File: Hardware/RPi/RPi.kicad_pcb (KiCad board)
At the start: 2 copper layers, 90 parts, among them P1 USB_B, P10 Solder_Pad, P11 Solder_Pad, P12 Solder_Pad, P13 Solder_Pad, P14 Solder_Pad, P15 Solder_Pad, P16 Solder_Pad, P17 Solder_Pad, P18 Solder_Pad, P19 Solder_Pad, P2 CONN_01X06, P3 USB_A, P4 USB_A, P5 USB_A, P6 USB_A, P7 Solder_Pad, P8 Solder_Pad, P9 Solder_Pad, U1 MPU_9150, U10 WS2812B, U11 WS2812B, U12 WS2812B, U13 Teensy_LC, U14 WS2812B, U15 WS2812B, U16 WS2812B, U17 WS2812B, U18 WS2812B, U19 WS2812B, U2 RPi_Interface, U3 FE1.1s, U4 AP1117E25, U5 Dual_buffer_NC7WZ16, U6 ESP-12E, U7 WS2812B, U8 WS2812B, U9 WS2812B, Y1 Crystal 12MHz

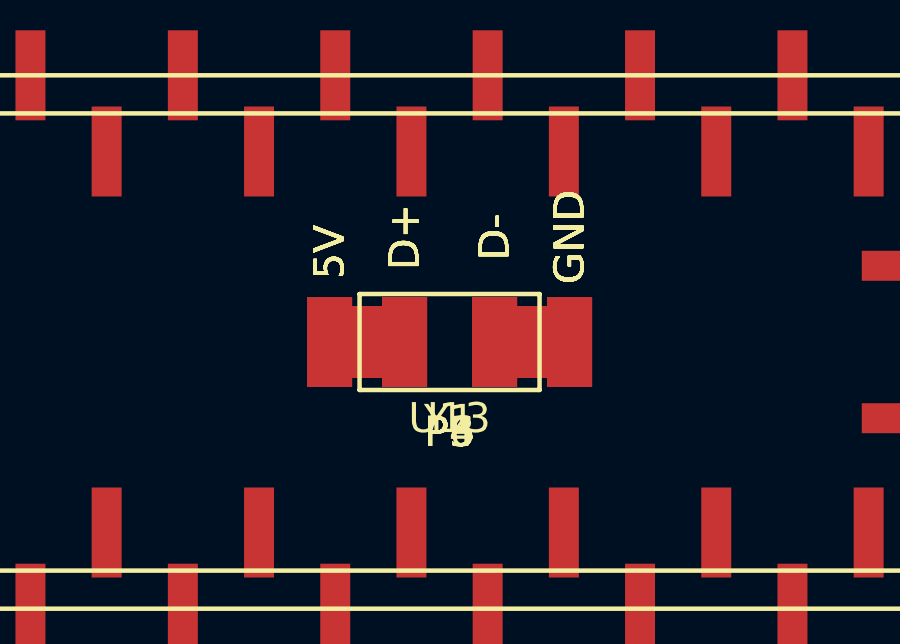
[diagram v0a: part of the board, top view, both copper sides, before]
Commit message: Fixed schematic/component errors
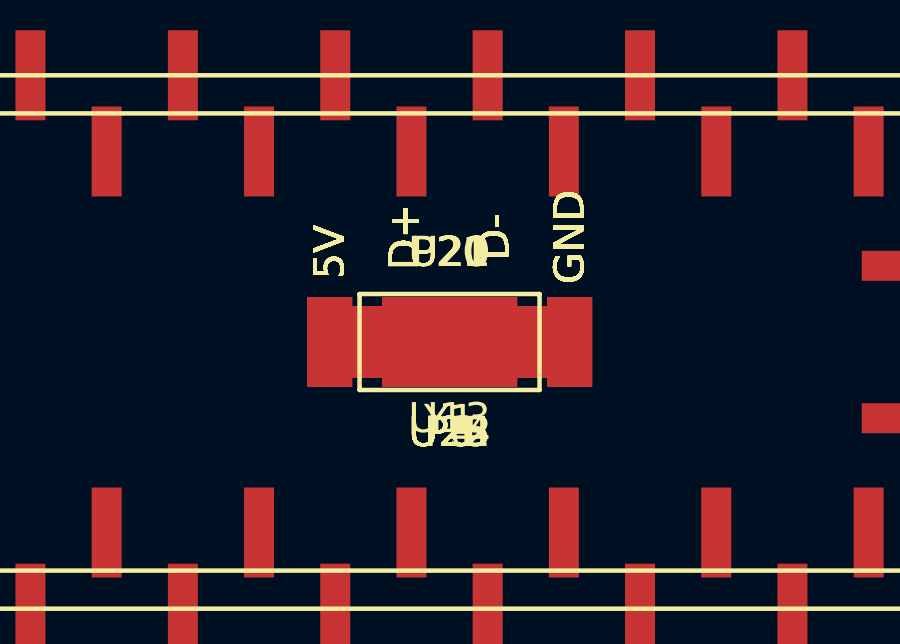
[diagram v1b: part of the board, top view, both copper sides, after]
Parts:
- added P20, P21: Solder_Pad, Measurement_Points:Measurement_Point_Square-SMD-Pad_Big, F.Cu at (0.00, 0.00)
- added U20, U21: SolderpadPowerOut, Measurement_Points:Measurement_Point_Square-SMD-Pad_Big, F.Cu at (0.00, 0.00)
- added U22, U23, U24, U25: USB_Solder_Pad, TimeArc:USB_A_SMD_Pads, F.Cu at (0.00, 0.00)
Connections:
- P1 pad 1: +5V -> Net-(P1-Pad1)
- P3 pad 4: GND -> Net-(P3-Pad4)
- P4 pad 4: GND -> Net-(P4-Pad4)
- P5 pad 4: GND -> Net-(P5-Pad4)
- P6 pad 4: GND -> Net-(P6-Pad4)
- R11 pad 2: Net-(R11-Pad2) -> Net-(P1-Pad1)
- R12 pad 2: Net-(R12-Pad2) -> GND
- R13 pad 2: Net-(R13-Pad2) -> GND
- U13 pad 0: Net-(P7-Pad1) -> (no net)
- U13 pad 1: Net-(P8-Pad1) -> GND
- U13 pad 10: UART_RX -> Net-(U13-Pad10)
- U13 pad 11: Net-(U13-Pad11) -> UART_TX
- U13 pad 12: Net-(U13-Pad12) -> UART_RX
- U13 pad 15: Net-(P19-Pad1) -> WS2812
- U13 pad 16: Net-(P18-Pad1) -> Net-(U13-Pad16)
- U13 pad 17: WS2812 -> GND
- U13 pad 18: Net-(P16-Pad1) -> Net-(U13-Pad18)
- U13 pad 2: Net-(U13-Pad2) -> Net-(P7-Pad1)
- U13 pad 22: Net-(P15-Pad1) -> Net-(P19-Pad1)
- U13 pad 23: Net-(P14-Pad1) -> Net-(P18-Pad1)
- U13 pad 24: (no net) -> Net-(P17-Pad1)
- U13 pad 25: (no net) -> Net-(P16-Pad1)
- U13 pad 27: (no net) -> Net-(U13-Pad27)
- U13 pad 28: (no net) -> Net-(U13-Pad28)
- U13 pad 3: Net-(P9-Pad1) -> Net-(P8-Pad1)
- U13 pad 32: (no net) -> GND
- U13 pad 33: (no net) -> +5V
- U13 pad 4: Net-(P10-Pad1) -> Net-(U13-Pad4)
- U13 pad 5: Net-(U13-Pad5) -> Net-(P9-Pad1)
- U13 pad 6: Net-(U13-Pad6) -> Net-(P10-Pad1)
- U13 pad 9: UART_TX -> Net-(U13-Pad9)
- U2 pad 17: +3V3 -> Net-(U2-Pad17)
- U3 pad 10: Net-(P4-Pad2) -> Net-(U22-Pad2)
- U3 pad 11: Net-(P4-Pad3) -> Net-(U22-Pad3)
- U3 pad 4: Net-(P3-Pad2) -> Net-(U23-Pad2)
- U3 pad 5: Net-(P3-Pad3) -> Net-(U23-Pad3)
- U3 pad 6: Net-(P6-Pad2) -> Net-(U25-Pad2)
- U3 pad 7: Net-(P6-Pad3) -> Net-(U25-Pad3)
- U3 pad 8: Net-(P5-Pad2) -> Net-(U24-Pad2)
- U3 pad 9: Net-(P5-Pad3) -> Net-(U24-Pad3)
- U4 pad 3: Net-(R11-Pad2) -> +5V

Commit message: Starting pcb layout
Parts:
- added REF**: MountingHole_3.2mm_M3_ISO7380, Mounting_Holes:MountingHole_3.2mm_M3_ISO7380, F.Cu at (12.0, 11.0)
- added REF**: MountingHole_3.2mm_M3_ISO7380, Mounting_Holes:MountingHole_3.2mm_M3_ISO7380, F.Cu at (12.0, 97.0)
- added REF**: MountingHole_3.2mm_M3_ISO7380, Mounting_Holes:MountingHole_3.2mm_M3_ISO7380, F.Cu at (98.0, 97.0)
- added REF**: MountingHole_3.2mm_M3_ISO7380, Mounting_Holes:MountingHole_3.2mm_M3_ISO7380, F.Cu at (98.0, 11.0)
- U10, U11, U12, U14, U15, U16, U17, U18, U19, U7, U8, U9: moved to B.Cu
- moved P21 270.4 mm to (269.7, 19.6)
- moved P5 249.1 mm to (249.1, 2.05)
- moved U22 237.9 mm to (237.8, 2.05)
- moved P6 237.0 mm to (236.4, 16.6)
- moved P20 233.4 mm to (226.0, 58.1)
- moved P4 227.1 mm to (226.5, 16.6)
- moved P3 211.9 mm to (208.1, 40.0)
- moved U25 211.3 mm to (209.5, 27.9)
- moved U23 200.9 mm to (194.9, 48.6)
- moved U24 192.6 mm to (182.5, 61.4)
- moved U20 182.2 mm to (175.4, 49.3)
- moved Y1 179.7 mm to (166.9, 66.5)
- moved U21 178.6 mm to (168.7, 58.7)
- moved C1 169.7 mm to (266.9, 26.6)
- moved C6 169.0 mm to (285.9, 6.67)
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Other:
- board outline added: 100 x 100 mm

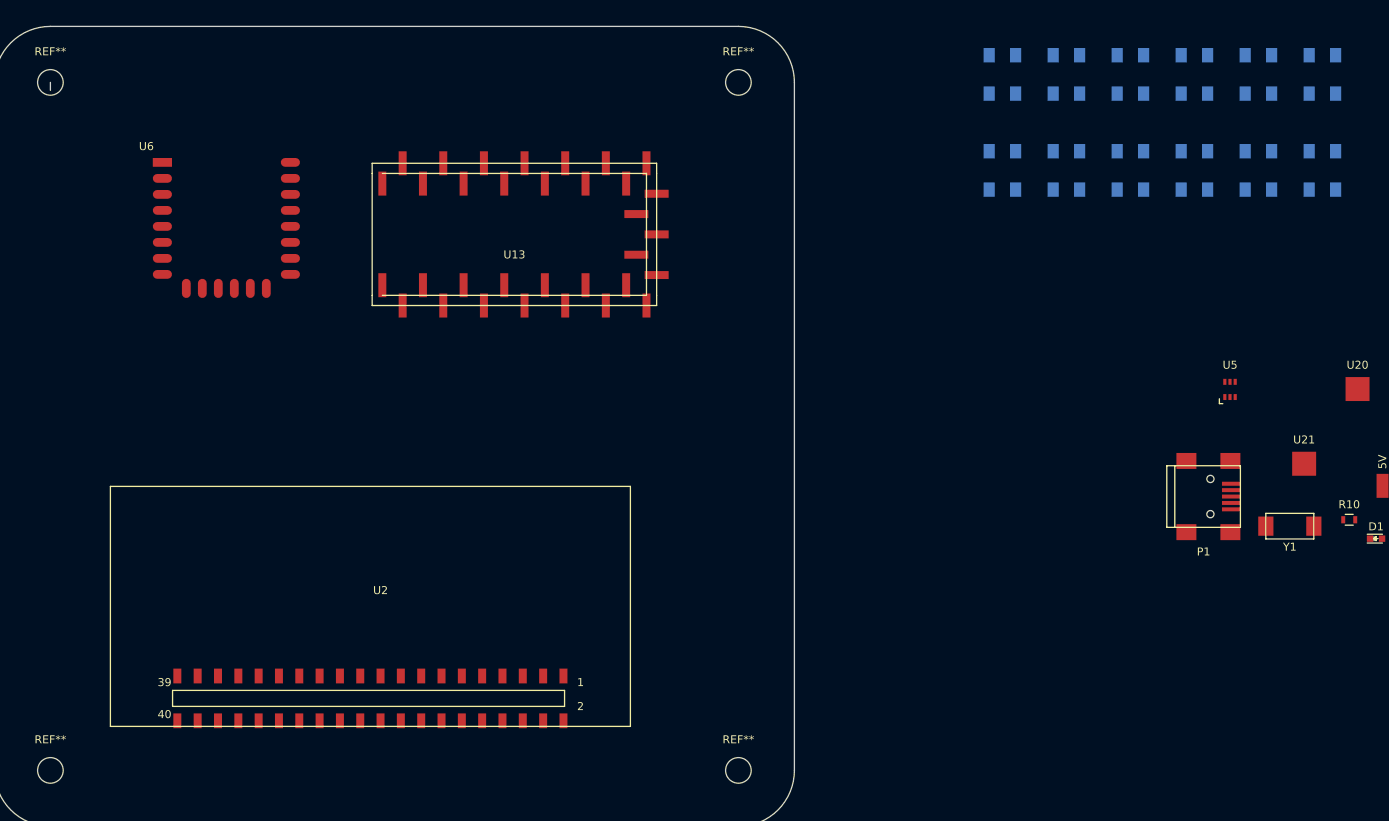
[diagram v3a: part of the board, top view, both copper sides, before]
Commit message: Placing the leds almost circular
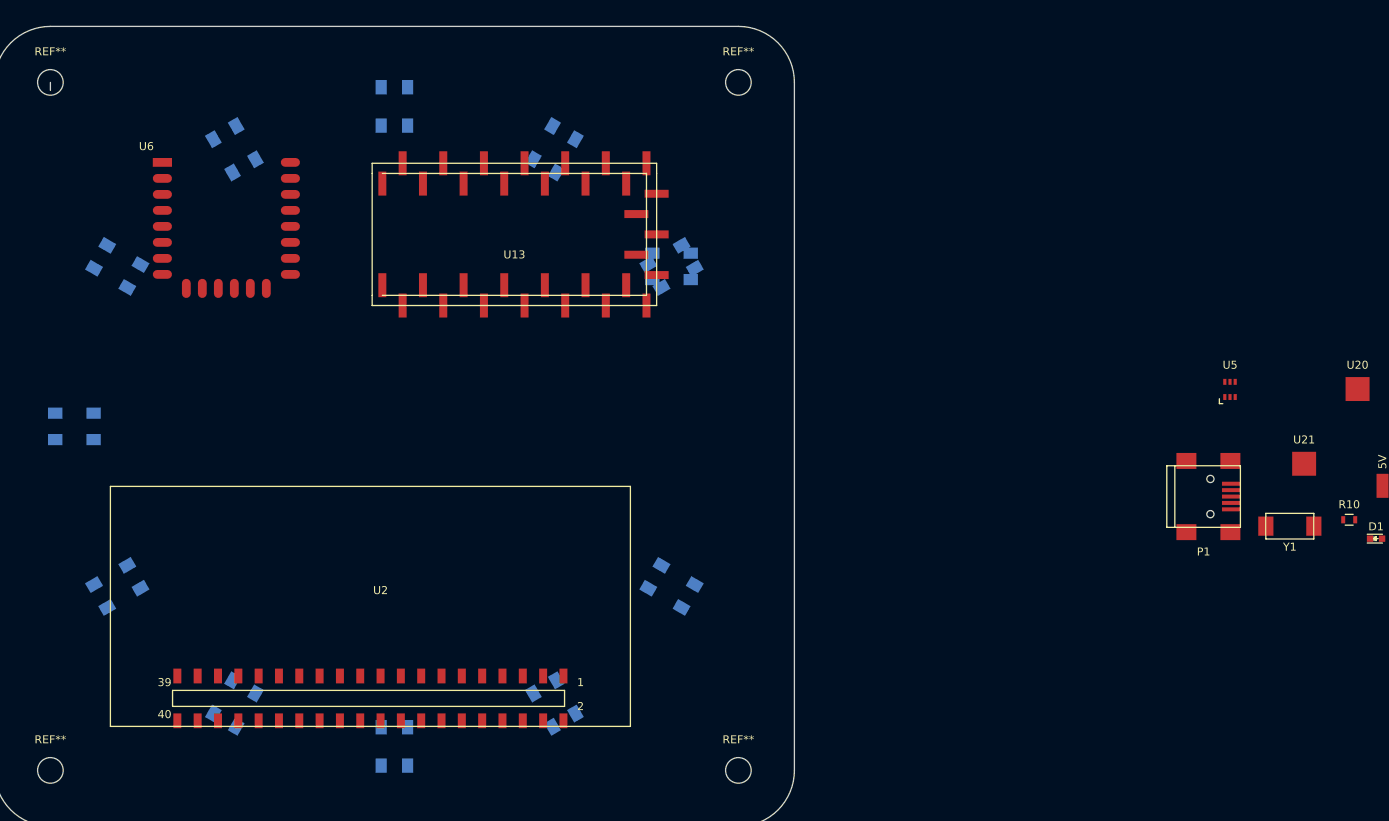
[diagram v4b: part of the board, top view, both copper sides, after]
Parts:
- moved U12 156.3 mm to (20.4, 74.0), turned to 300 degrees
- moved U14 151.4 mm to (15.0, 54.0), turned to 270 degrees
- moved U16 136.3 mm to (35.0, 19.4), turned to 210 degrees
- moved U15 119.2 mm to (20.4, 34.0), turned to 240 degrees
- moved U11 116.9 mm to (35.0, 88.6), turned to 330 degrees
- moved U10 116.8 mm to (55.0, 94.0)
- moved U9 104.1 mm to (75.0, 88.6), turned to 30 degrees
- moved U17 92.1 mm to (55.0, 14.0), turned to 180 degrees
- moved U8 91.5 mm to (89.6, 74.0), turned to 60 degrees
- moved U19 82.2 mm to (89.6, 34.0), turned to 120 degrees
- moved U18 56.8 mm to (75.0, 19.4), turned to 150 degrees
- moved U7 54.9 mm to (89.6, 34.0), turned to 90 degrees

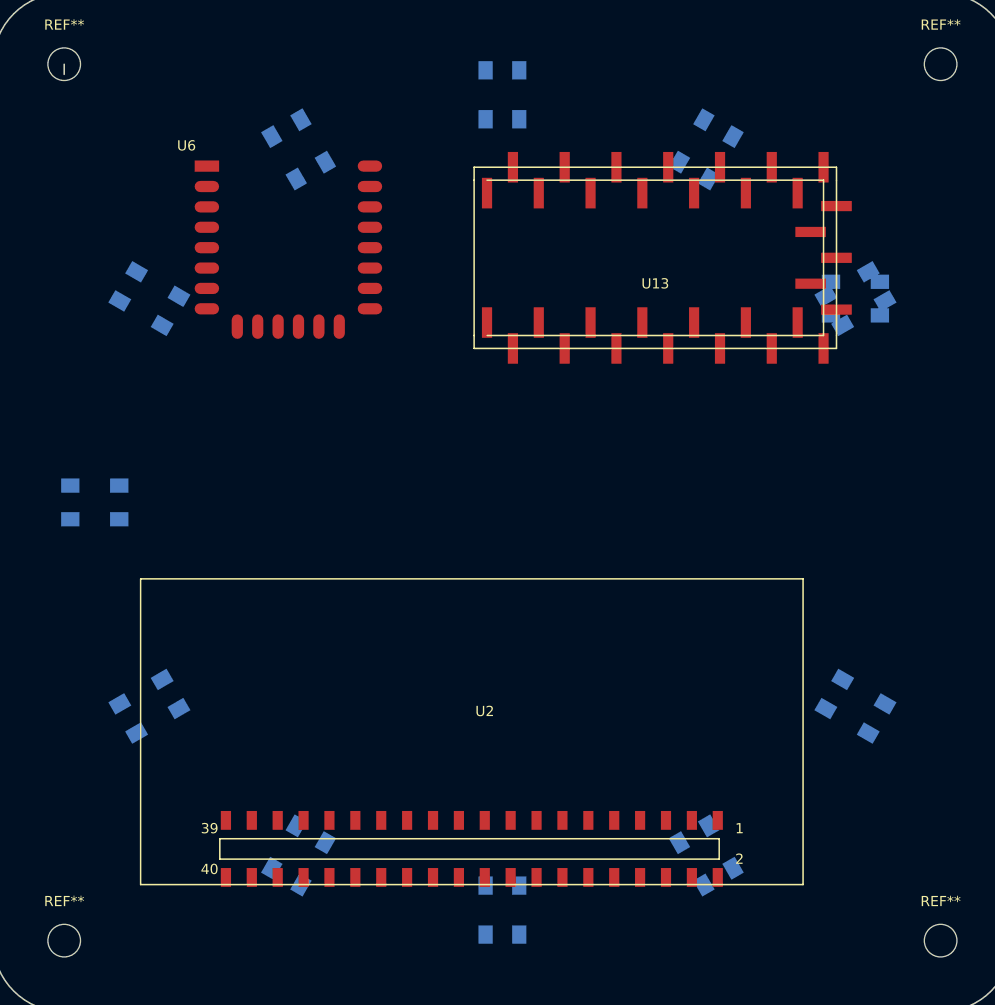
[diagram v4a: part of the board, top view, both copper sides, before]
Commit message: Fixed first leds position wrong (Dirty hack)
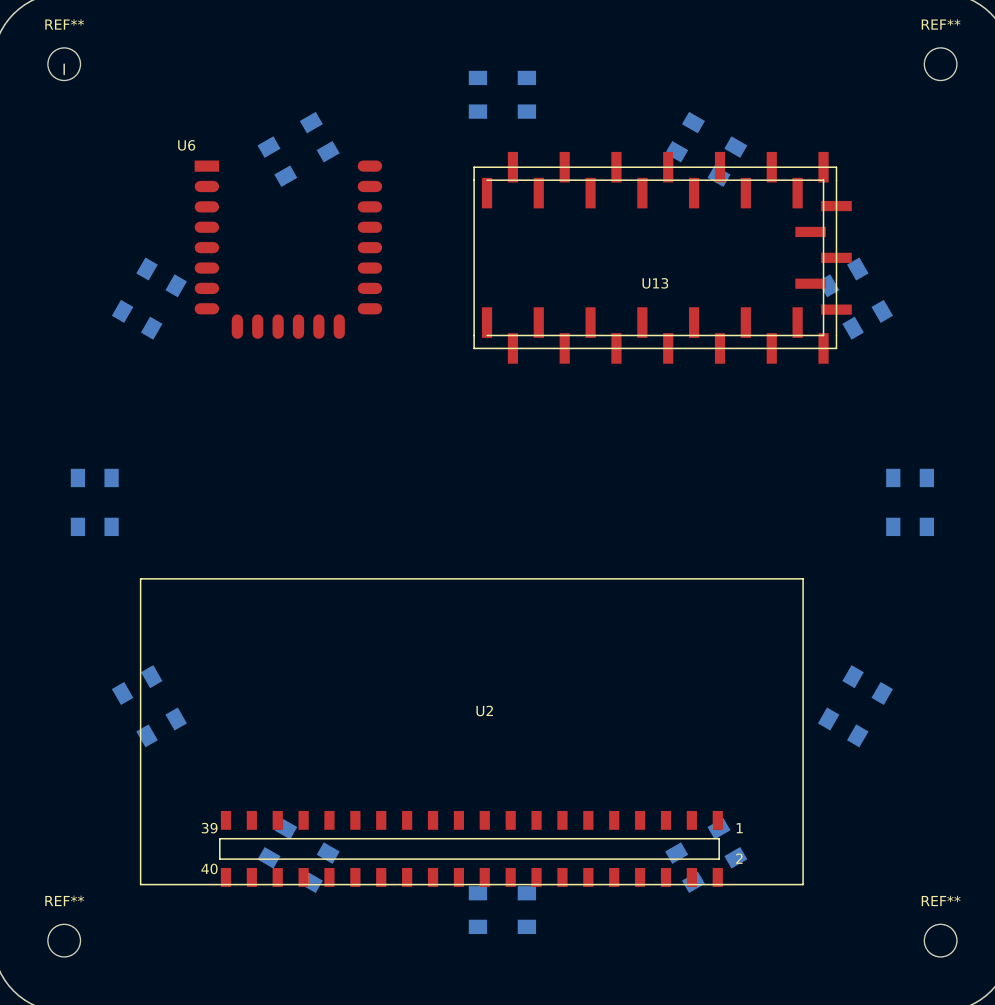
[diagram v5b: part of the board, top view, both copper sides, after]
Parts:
- moved U7 20.7 mm to (95.0, 54.0), turned to 0 degrees
- turned U10 to 270 degrees
- turned U11 to 240 degrees
- turned U12 to 210 degrees
- turned U14 to 180 degrees
- turned U15 to 150 degrees
- turned U16 to 120 degrees
- turned U17 to 90 degrees
- turned U18 to 60 degrees
- turned U19 to 30 degrees
- turned U8 to 330 degrees
- turned U9 to 300 degrees

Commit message: Removed FTDI header, removed all unused footprints
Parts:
- removed P4, P5, P6: USB_A, TimeArc:USB_A_SMD_Pads
- P2: value CONN_01X06 -> Solder_Pad; footprint TimeArc:1x06 pinheader smd -> Measurement_Points:Measurement_Point_Square-SMD-Pad_Big
- P3: value USB_A -> Solder_Pad
- moved U3 188.5 mm to (51.0, 70.0)
- moved P2 164.3 mm to (50.0, 110.1)
- moved P3 157.9 mm to (51.0, 56.0)
- moved U23 157.1 mm to (38.0, 56.0)
- moved U25 148.2 mm to (64.0, 56.0)
- moved P1 132.2 mm to (24.0, 59.0), turned to 270 degrees
- moved U24 106.7 mm to (76.0, 56.0)
- moved U6 11.2 mm to (21.0, 11.0)
- moved U19 6.40 mm to (84.6, 30.0)
- moved U16 6.40 mm to (30.0, 15.4)
- moved REF** 6.40 mm to (7.00, 7.00)
- moved REF** 6.40 mm to (7.00, 93.0)
- moved REF** 6.40 mm to (93.0, 93.0)
- moved REF** 6.40 mm to (93.0, 7.00)
- moved U10 6.40 mm to (50.0, 90.0)
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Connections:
- P3 pad 1: +5V -> Net-(P3-Pad1)
- P3 pad 2: Net-(P3-Pad2) -> (no net)
- P3 pad 3: Net-(P3-Pad3) -> (no net)
- P3 pad 4: Net-(P3-Pad4) -> (no net)
- U13 pad 10: Net-(U13-Pad10) -> Net-(P3-Pad1)
- U13 pad 9: Net-(U13-Pad9) -> Net-(P2-Pad1)

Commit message: Placing stuff on the board
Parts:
- added P4: Solder_Pad, Measurement_Points:Measurement_Point_Square-SMD-Pad_Big, F.Cu at (73.0, 43.0)
- P3: footprint TimeArc:USB_A_SMD_Pads -> Measurement_Points:Measurement_Point_Square-SMD-Pad_Big
- U5: footprint TO_SOT_Packages_SMD:SC-70-6 -> TO_SOT_Packages_SMD:SC-70-6_Handsoldering
- moved P21 210.8 mm to (65.0, 70.0)
- moved P19 199.0 mm to (84.0, 34.0)
- moved P14 197.4 mm to (52.0, 34.0)
- moved U22 194.5 mm to (51.0, 56.0)
- moved P12 192.6 mm to (83.0, 41.0)
- moved P17 192.6 mm to (76.0, 34.0)
- moved P13 192.0 mm to (69.0, 43.0)
- moved P7 186.9 mm to (44.0, 34.0)
- moved P9 184.4 mm to (56.0, 34.0)
- moved P15 178.9 mm to (60.0, 34.0)
- moved P18 178.8 mm to (80.0, 34.0)
- moved U4 176.9 mm to (78.0, 66.0)
- moved P10 166.0 mm to (64.0, 34.0)
- moved P8 160.0 mm to (48.0, 34.0)
- moved P20 157.5 mm to (69.0, 70.0)
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
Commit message: Removed USB hub, ordered pcb
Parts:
- removed C1, C3, C4, C6: 10u, Capacitors_SMD:C_0603
- removed C2, C7: 100n, Capacitors_SMD:C_0603
- removed D1, D2, D3, D4, D5: LED, LEDs:LED_0603
- removed P1: USB_B, Connect:USB_Mini-B
- removed R1: 100k, Resistors_SMD:R_0603
- removed R11: 0, Resistors_SMD:R_0603
- removed R2: 47k, Resistors_SMD:R_0603
- removed R3: 2.7k, Resistors_SMD:R_0603
- removed R5, R6, R7: 330, Resistors_SMD:R_0603
- removed U22, U23, U24, U25: USB_Solder_Pad, TimeArc:USB_A_SMD_Pads
- removed U3: FE1.1s, Housings_SSOP:SSOP-28_5.3x10.2mm_Pitch0.65mm
- removed Y1: Crystal 12MHz, TimeArc:Crystal_12MHz
- added REF**: 1pin, Connect:1pin, F.Cu at (47.5, 52.0)
- moved C11 263.3 mm to (21.0, 38.0), turned to 270 degrees
- moved C15 244.6 mm to (40.5, 69.5), turned to 90 degrees
- moved R14 241.3 mm to (23.5, 38.0), turned to 90 degrees
- moved R12 240.9 mm to (43.5, 82.0), turned to 270 degrees
- moved R26 240.8 mm to (42.5, 26.0)
- moved R23 233.6 mm to (53.0, 69.5), turned to 90 degrees
- moved R18 224.4 mm to (33.5, 38.0), turned to 270 degrees
- moved R15 224.3 mm to (26.0, 38.0), turned to 90 degrees
- moved R17 223.5 mm to (31.0, 38.0), turned to 90 degrees
- moved R4 218.5 mm to (69.0, 66.5), turned to 270 degrees
- moved R16 215.3 mm to (28.5, 38.0), turned to 90 degrees
- moved C8 208.0 mm to (69.0, 77.0), turned to 270 degrees
- moved R19 201.1 mm to (36.0, 38.0), turned to 90 degrees
- moved C16 197.5 mm to (50.5, 69.5), turned to 90 degrees
- moved C14 195.2 mm to (53.5, 77.0), turned to 270 degrees
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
